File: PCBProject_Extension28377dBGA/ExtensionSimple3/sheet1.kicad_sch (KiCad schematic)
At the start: 124 parts, among them J1 Conn_02x05_Odd_Even, J1 Conn_02x08_Top_Bottom, J2 Conn_01x02_Pin, J6 Conn_02x05_Odd_Even, Q1 FMMT618TA, U1 SN74ABT541, U2 SN74ABT541

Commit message: fix SCI_C AND D, ADD ECAP TO 1TO2
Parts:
- added UART5, UART6: Conn_01x06, Connector_PinHeader_2.54mm:PinHeader_1x06_P2.54mm_Vertical, symbol Connector_Generic:Conn_01x06
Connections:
- net A+5V: now also UART5.4 (Pin_4), UART6.4 (Pin_4)
- net AGND: now also UART5.6 (Pin_6), UART6.6 (Pin_6)
- net ECAP1_IPM_TerminalDutyU1: now also UART5.1 (Pin_1)
- net ECAP2_IPM_TerminalDutyV1: now also UART5.2 (Pin_2)
- net ECAP3_IPM_TerminalDutyW1: now also UART5.3 (Pin_3)
- net ECAP4_IPM_TerminalDutyU2: now also UART6.1 (Pin_1)
- net ECAP5_IPM_TerminalDutyV2: now also UART6.2 (Pin_2)
- net ECAP6_IPM_TerminalDutyW2: now also UART6.3 (Pin_3)
- net UART_SCI_RXDC: now also DSP2.120 (A1_120); no longer DSP2.107 (107_D3)
- net UART_SCI_RXDD: now also DSP2.110 (A6_110); no longer DSP2.105 (105_D4)
- net UART_SCI_TXDC: now also DSP2.122 (A0_122); no longer DSP2.106 (A8_106)
- net UART_SCI_TXDD: now also DSP2.108 (A7_108); no longer DSP2.104 (A9_104)
- net VDD: now also UART5.5 (Pin_5), UART6.5 (Pin_5)
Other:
- note added: "ECAP"
- note added: "GP38"
- note added: "GP39"
- note added: "GP46"
- note added: "GP47"
- note removed: "GP104"
- note removed: "GP105"
- note removed: "GP106"
- note removed: "GP107"

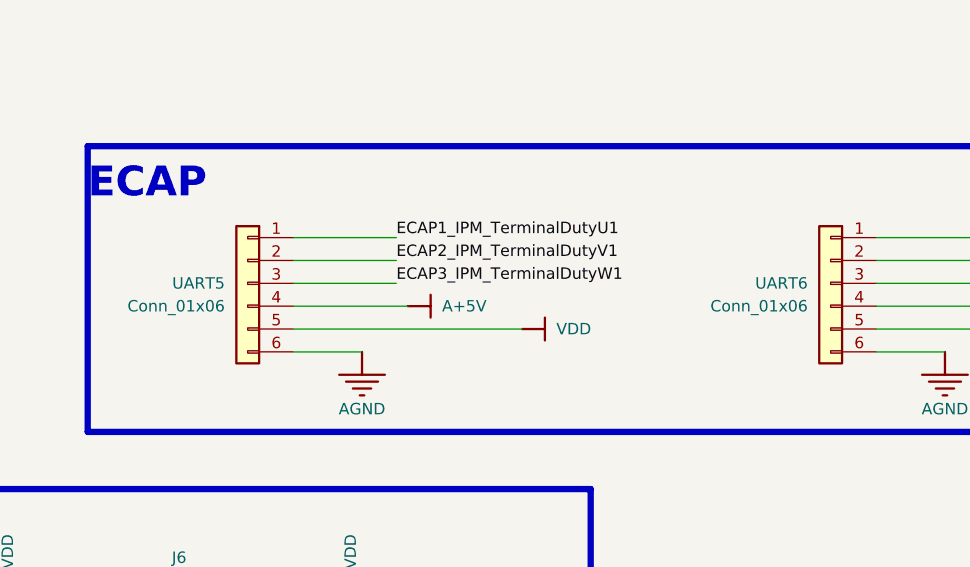
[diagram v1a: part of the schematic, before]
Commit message: fix SCI_C and D, add ECAP to 1TO4, but 1TO4 haven't finish.
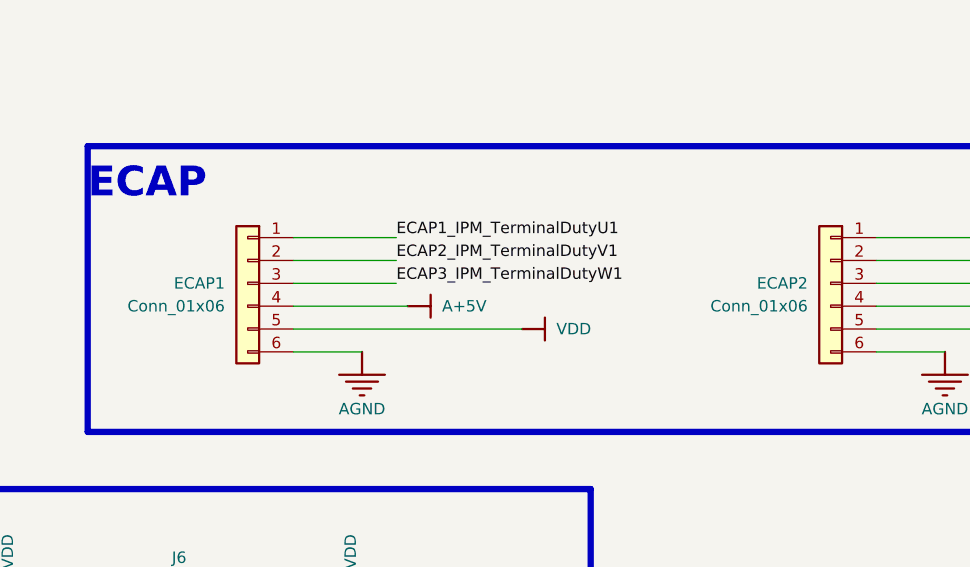
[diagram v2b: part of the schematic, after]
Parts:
- renumbered UART5 to ECAP1, UART6 to ECAP2
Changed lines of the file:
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@@
   (symbol (lib_id "Connector_Generic:Conn_01x06") (at 952.5 386.08 0) (mirror y) (unit 1)
     (in_bom yes) (on_board yes) (dnp no)
-    (property "Reference" "UART6" (at 949.96 386.08 0)
+    (property "Reference" "ECAP2" (at 949.96 386.08 0)
       (effects (font (size 1.27 1.27)) (justify left))
     )
@@
       (project "sheet1"
         (path "/54840d93-b842-4275-b1cb-4ec5510cbfff"
-          (reference "UART6") (unit 1)
+          (reference "ECAP2") (unit 1)
         )
       )
@@
   (symbol (lib_id "Connector_Generic:Conn_01x06") (at 887.73 386.08 0) (mirror y) (unit 1)
     (in_bom yes) (on_board yes) (dnp no)
-    (property "Reference" "UART5" (at 885.19 386.08 0)
+    (property "Reference" "ECAP1" (at 885.19 386.08 0)
       (effects (font (size 1.27 1.27)) (justify left))
     )
@@
       (project "sheet1"
         (path "/54840d93-b842-4275-b1cb-4ec5510cbfff"
-          (reference "UART5") (unit 1)
-        )
-      )
+          (reference "ECAP1") (unit 1)
+        )
+      )

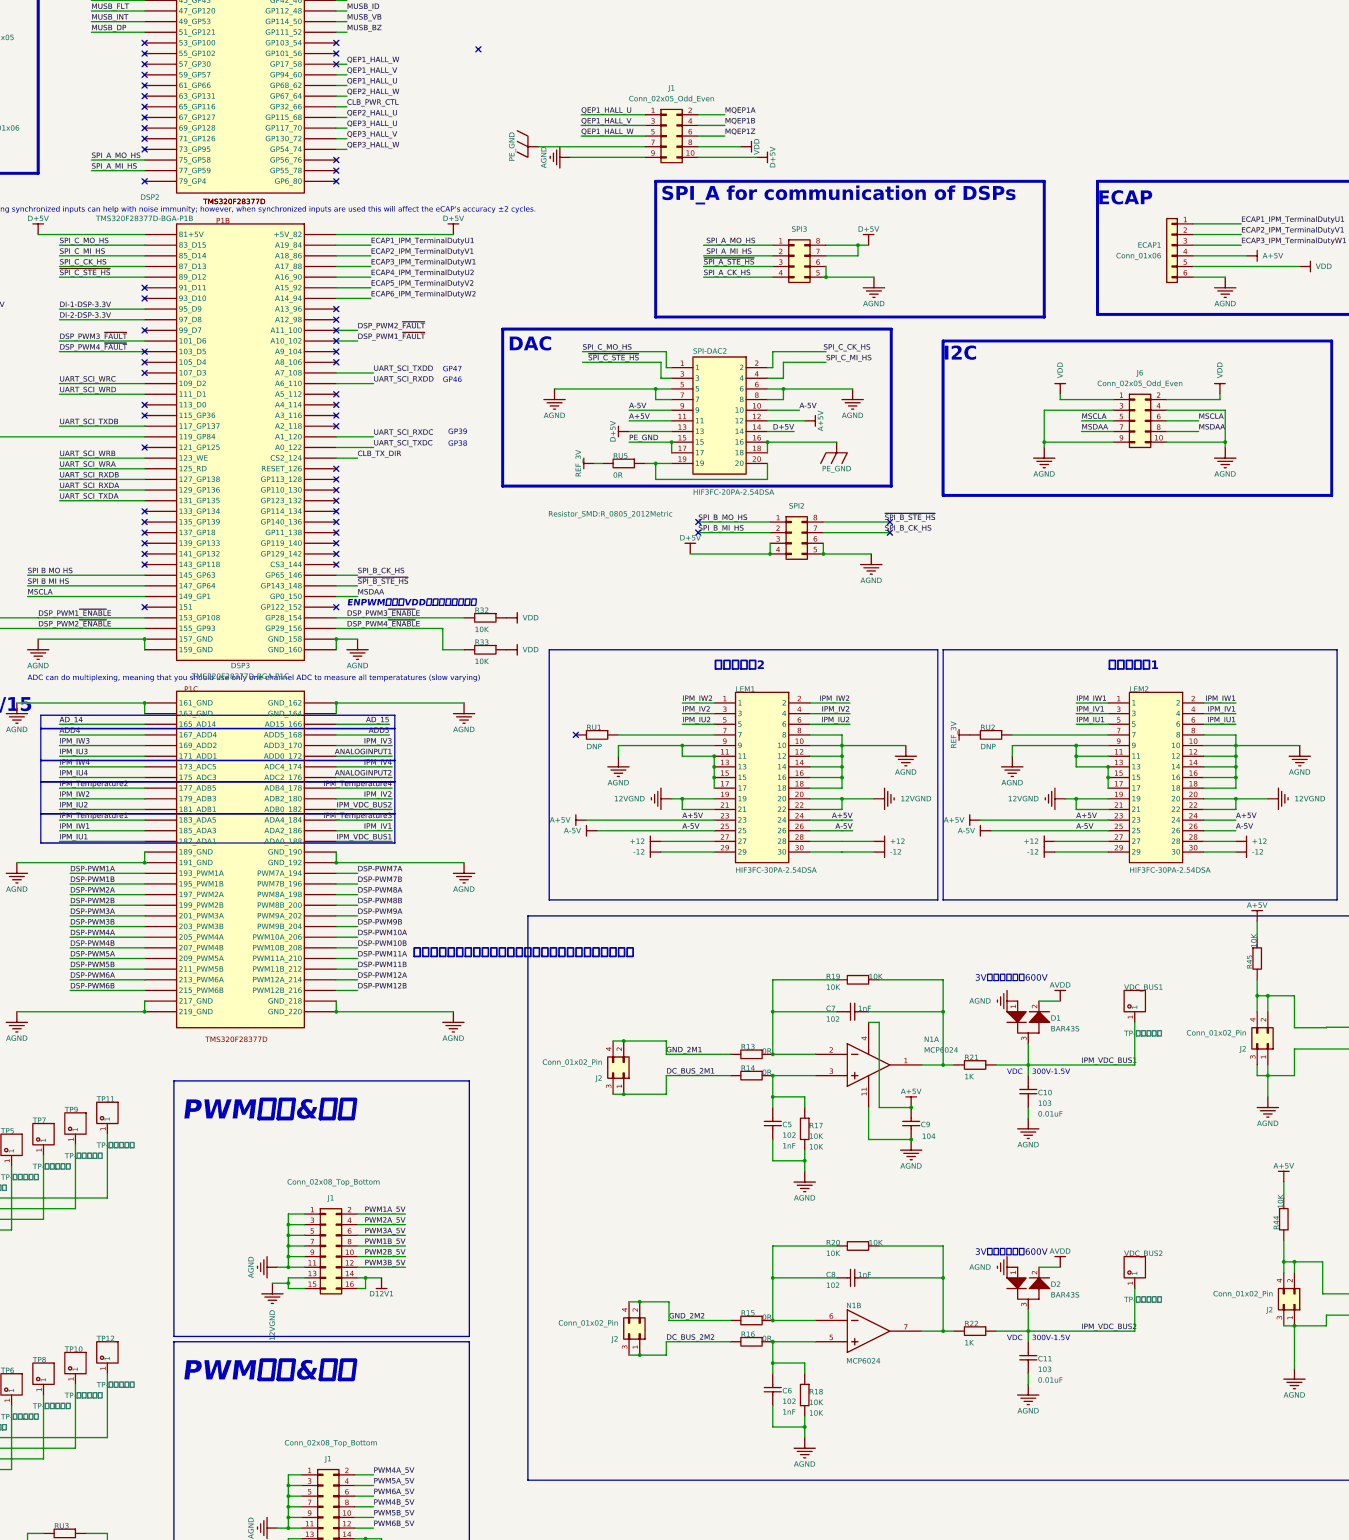
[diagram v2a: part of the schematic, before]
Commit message: 修改SPI-B为高速SPIGPIO
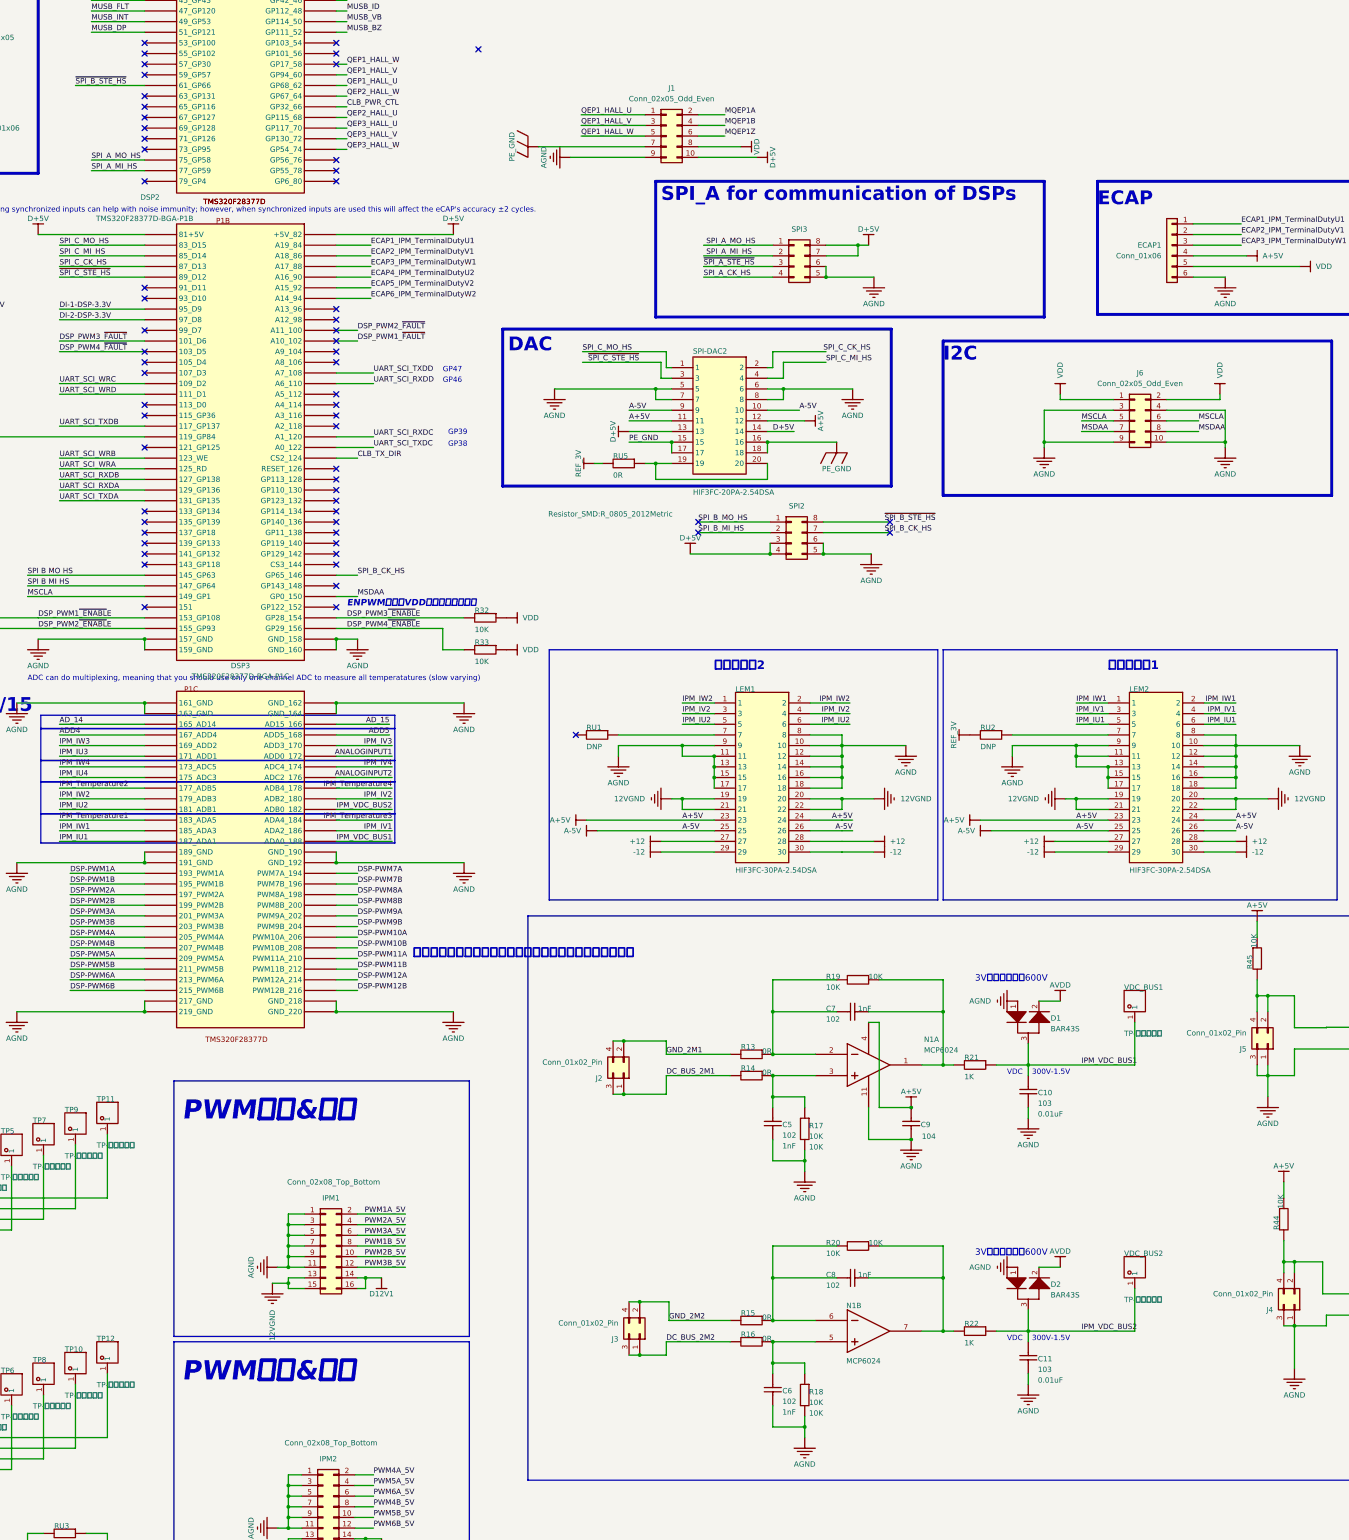
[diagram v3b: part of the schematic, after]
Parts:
- renumbered J1 to IPM1, J1 to IPM2, J2 to J3, J2 to J4, J2 to J5
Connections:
- net ~{SPI_B_STE_HS}: now also DSP1.61 (61_GP66); no longer DSP2.148 (GP143_148)

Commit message: 添加ADC拓展板
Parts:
- added J7: Conn_01x20, symbol Connector_Generic:Conn_01x20
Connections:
- net A+5V: now also J7.18 (Pin_18)
- net ADD4: now also J7.3 (Pin_3)
- net ADD5: now also J7.4 (Pin_4)
- net AD_14: now also J7.1 (Pin_1)
- net AD_15: now also J7.2 (Pin_2)
- net AGND: now also J7.20 (Pin_20)
- net AVDD: now also J7.19 (Pin_19)
- net IPM_IU3 renamed ADD1
- net ADD1: now also J7.7 (Pin_7)
- net IPM_IU4 renamed ADC3
- net ADC3: now also J7.10 (Pin_10)
- net IPM_IV3 renamed ADD3
- net ADD3: now also J7.6 (Pin_6)
- net IPM_IV4 renamed ADC4
- net ADC4: now also J7.9 (Pin_9)
- net IPM_IW3 renamed ADD2
- net ADD2: now also J7.5 (Pin_5)
- net IPM_IW4 renamed ADC5
- net ADC5: now also J7.8 (Pin_8)
- net IPM_Temperature1 renamed ADA5
- net ADA5: now also J7.13 (Pin_13)
- net IPM_Temperature2 renamed ADB5
- net ADB5: now also J7.11 (Pin_11)
- net IPM_Temperature3 renamed ADA4
- net ADA4: now also J7.14 (Pin_14)
- net IPM_Temperature4 renamed ADB4
- net ADB4: now also J7.12 (Pin_12)
- no-connect marks 80 -> 82
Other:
- note added: "ADC拓展"
- moved on the sheet: C16, R41, R44, R45

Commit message: 添加绝对值编码器接口和IPM接口
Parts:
- removed C1, C2: 104, Capacitor_SMD:C_0805_2012Metric, symbol sheet1-altium-import:root_1_Cap
- removed C3, C4: 104, Capacitor_SMD:C_0805_2012Metric, symbol sheet1-altium-import:root_0_Cap
- removed IPM1, IPM2: Conn_02x08_Top_Bottom, Connector_PinSocket_2.54mm:PinSocket_2x08_P2.54mm_Vertical, symbol Connector_Generic:Conn_02x08_Odd_Even
- removed LEM1, LEM2: HIF3FC-30PA-2.54DSA, Connector_PinSocket_2.54mm:PinSocket_2x15_P2.54mm_Vertical, symbol sheet1-altium-import:root_0_HIF3FC-30PA-2.54DSA
- removed R1, R10, R11, R12, R2, R3, R4, R7, R8, R9: 4.7k, Resistor_SMD:R_0805_2012Metric, symbol sheet1-altium-import:root_1_Res2
- removed R5, R6: 4.7K, Resistor_SMD:R_0805_2012Metric, symbol sheet1-altium-import:root_1_Res2
- removed RU1, RU2: DNP, Resistor_SMD:R_0805_2012Metric, symbol sheet1-altium-import:root_0_Res2
- removed TP1, TP10, TP11, TP12, TP2, TP3, TP4, TP5, TP6, TP7, TP8, TP9: ${MANUFACTURER PART}, TestPoint:TestPoint_Pad_2.0x2.0mm, symbol sheet1-altium-import:root_1_TP-黄色测试点
- removed U1, U2: SN74ABT541, 1mmlab_footprint:TSSOP-20, symbol sheet1-altium-import:root_0_SN74ABT541
- added C134: 0.1uF/50V, Capacitor_SMD:C_0603_1608Metric, symbol sheet1-altium-import:CAP_2
- added DSUB5, DSUB6: DMR-9S, Lib_sheet_10:DSUB-TH_DMR-9S, symbol sheet1-altium-import:DMR-9S
- added X1: 20MHz, Lib_sheet_10:OSC-SMD_4P-L2.5-W2.0-BL, symbol sheet1-altium-import:ECS-2520S33-250-FN-TR
- renumbered R27 to R289, R28 to R290
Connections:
- net AGND: now also C134.2, DSUB5.9, DSUB6.9, X1.2 (Gnd)
- net D+5V: now also DSUB5.1, DSUB6.1
- net PE_GND: now also DSUB5.10 (MH1), DSUB5.11 (MH2), DSUB6.10 (MH1), DSUB6.11 (MH2)
- net VDD: now also C134.1, X1.4 (Vdd)
- new net ADC_CLK_X1: X1.3 (Output)
- new net RS485-C+_1: DSUB5.5, DSUB6.5
- new net RS485-C-_1: DSUB5.4, DSUB6.4
- new net RS485-D+_1: DSUB5.3, DSUB6.3
- new net RS485-D-_1: DSUB5.2, DSUB6.2
- no-connect marks 82 -> 86
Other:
- added sheet IPM1 (IPM.kicad_sch)
- added sheet IPM2 (IPM.kicad_sch)
- added sheet 绝对值编码器1 (绝对值编码器.kicad_sch)
- added sheet 绝对值编码器2 (绝对值编码器.kicad_sch)
- note added: "ENPWM默认封波"
- note added: "PWM 使能 报错 ，ADC电流 电压 温度 ,刹车发波"
- note added: "电流采样用的20MHz时钟"
- note added: "绝对值编码器CLB实现多摩川协议tformat）（本质上是用SPI外外设实现的！"
- note removed: "PWM信号&供电"
- note removed: "电平转换 From DSP 3.3V to 5V"
- note removed: "电流传感器1"
- note removed: "电流传感器2"
- moved on the sheet: J7, RU3
